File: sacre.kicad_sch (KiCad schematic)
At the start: 57 parts, among them J1 Touch, J2 Screen, M1 Vibration_Motor, Q1 CJ2312, Q2 S8050, Q3 CJ3415, Q4 SI1308EDL, U1 LIS3DH, U2 ESP32-PICO-D4, Y1 RV-8803-C7-TA-QC

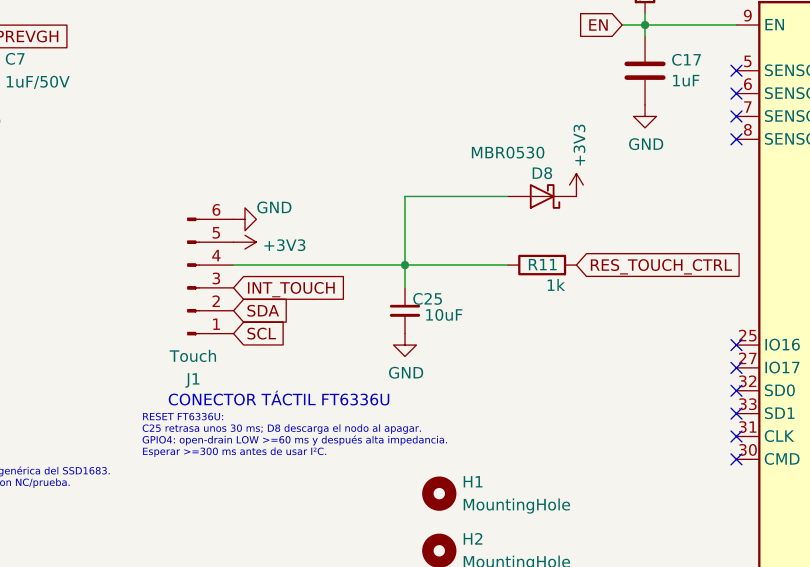
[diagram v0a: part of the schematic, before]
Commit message: Cierra revision PCB y prepara pedido JLCPCB
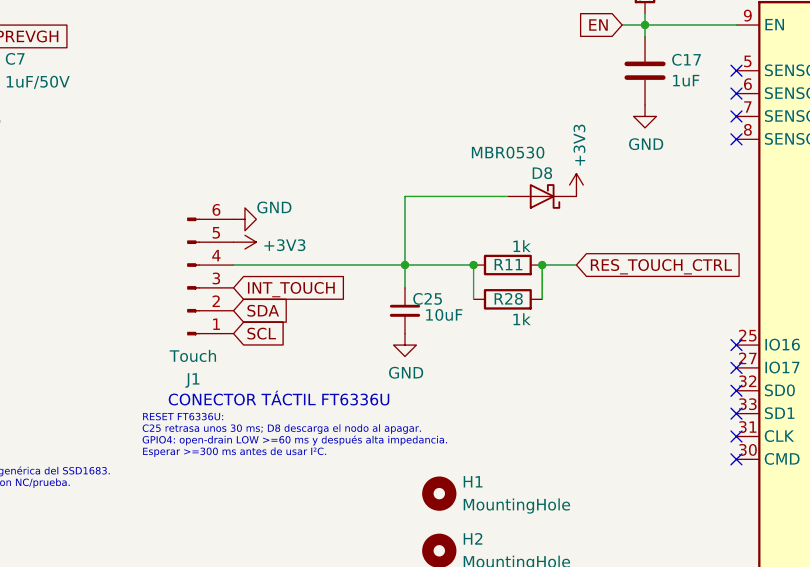
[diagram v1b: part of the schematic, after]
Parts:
- added R28: 1k, Resistor_SMD:R_0603_1608Metric, symbol SmartFeedback-rescue:R-Device
- M1: now left out of the parts list
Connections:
- net RES_TOUCH_CTRL: now also R28.2
- net at C25.1, D8.2 (A), J1.4 (Pin_4)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: now also R28.1
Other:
- moved on the sheet: R11
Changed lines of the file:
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@@
 	)
 	(junction
+		(at 199.39 110.49)
+		(diameter 0)
+		(color 0 0 0 0)
+	)
+	(junction
+		(at 191.77 110.49)
+		(diameter 0)
+		(color 0 0 0 0)
+	)
+	(junction
 		(at 38.1 59.69)
 		(diameter 0)
@@
 	(wire
 		(pts
+			(xy 191.77 110.49) (xy 191.77 114.3)
+		)
+		(stroke
+			(width 0)
+			(type default)
+		)
+	)
+	(wire
+		(pts
 			(xy 191.77 55.88) (xy 190.5 55.88)
 		)
@@
 	(wire
 		(pts
+			(xy 199.39 110.49) (xy 199.39 114.3)
+		)
+		(stroke
+			(width 0)
+			(type default)
+		)
+	)
+	(wire
+		(pts
 			(xy 54.61 109.22) (xy 57.15 109.22)
 		)
@@
 	(wire
 		(pts
+			(xy 199.39 110.49) (xy 203.2 110.49)
+		)
+		(stroke
+			(width 0)
+			(type default)
+		)
+	)
+	(wire
+		(pts
 			(xy 264.16 119.38) (xy 261.62 119.38)
 		)
@@
 	(wire
 		(pts
-			(xy 165.1 110.49) (xy 195.58 110.49)
+			(xy 165.1 110.49) (xy 191.77 110.49)
 		)
 		(stroke
@@
 		(body_style 1)
 		(exclude_from_sim no)
-		(in_bom yes)
+		(in_bom no)
 		(on_board yes)
-		(in_pos_files yes)
+		(in_pos_files no)
 		(dnp no)
 		(property "Reference" "M1"
@@
 	)
 	(symbol
+		(lib_id "SmartFeedback-rescue:R-Device")
+		(at 195.58 114.3 90)
+		(unit 1)
+		(body_style 1)
+		(exclude_from_sim no)
+		(in_bom yes)
+		(on_board yes)
+		(in_pos_files yes)
+		(dnp no)
+		(property "Reference" "R28"
+			(at 197.358 114.3 90)
+			(show_name no)
+			(do_not_autoplace no)
+			(effects
+				(font
+					(size 1.27 1.27)
+				)
+				(justify left)
+			)
+		)
+		(property "Value" "1k"
+			(at 198.12 116.586 90)
+			(show_name no)
+			(do_not_autoplace no)
+			(effects
+				(font
+					(size 1.27 1.27)
+				)
+				(justify left)
+			)
+		)
+		(property "Footprint" "Resistor_SMD:R_0603_1608Metric"
+			(at 195.58 116.078 0)
+			(hide yes)
+			(show_name no)
+			(do_not_autoplace no)
+			(effects
+				(font
+					(size 1.27 1.27)
+				)
+			)
+		)
+		(property "Datasheet" ""
+			(at 195.58 114.3 0)
+			(hide yes)
+			(show_name no)
+			(do_not_autoplace no)
+			(effects
+				(font
+					(size 1.27 1.27)
+				)
+			)
+		)
+		(property "Description" ""
+			(at 195.58 114.3 0)
+			(show_name no)
+			(do_not_autoplace no)
+			(effects
+				(font
+					(size 1.27 1.27)
+				)
+			)
+		)
+		(property "LCSC Part #" "C21190"
+			(at -3.81 3.81 0)
+			(hide yes)
+			(show_name no)
+			(do_not_autoplace no)
+			(effects
+				(font
+					(size 1.27 1.27)
+				)
+			)
+		)
+		(pin "1"
+		)
+		(pin "2"
+		)
+		(instances
+			(project "sacre"
+				(path "/a534c633-82b0-4919-83c8-539188551505"
+					(reference "R28")
+					(unit 1)
+				)
+			)
+		)
+	)
+	(symbol
 		(lib_id "SmartFeedback-rescue:GND-power")
 		(at 73.66 167.64 180)
@@
 	(symbol
 		(lib_id "SmartFeedback-rescue:R-Device")
-		(at 199.39 110.49 90)
+		(at 195.58 110.49 90)
 		(unit 1)
 		(body_style 1)
@@
 		(dnp no)
 		(property "Reference" "R11"
-			(at 201.168 110.49 90)
+			(at 197.358 110.49 90)
 			(show_name no)
 			(do_not_autoplace no)
@@
 		)
 		(property "Value" "1k"
-			(at 201.93 112.776 90)
+			(at 198.12 108.458 90)
 			(show_name no)
 			(do_not_autoplace no)
@@
 		)
 		(property "Footprint" "Resistor_SMD:R_0603_1608Metric"
-			(at 199.39 112.268 0)
+			(at 195.58 112.268 0)
 			(hide yes)
 			(show_name no)
@@
 		)
 		(property "Datasheet" ""
-			(at 199.39 110.49 0)
+			(at 195.58 110.49 0)
 			(hide yes)
 			(show_name no)
@@
 		)
 		(property "Description" ""
-			(at 199.39 110.49 0)
+			(at 195.58 110.49 0)
 			(show_name no)
 			(do_not_autoplace no)
@@
 		)
 		(property "LCSC Part #" "C21190"
-			(at 0 0 0)
+			(at -3.81 0 0)
 			(hide yes)
 			(show_name no)
